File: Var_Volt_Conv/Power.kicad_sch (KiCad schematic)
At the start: 64 parts

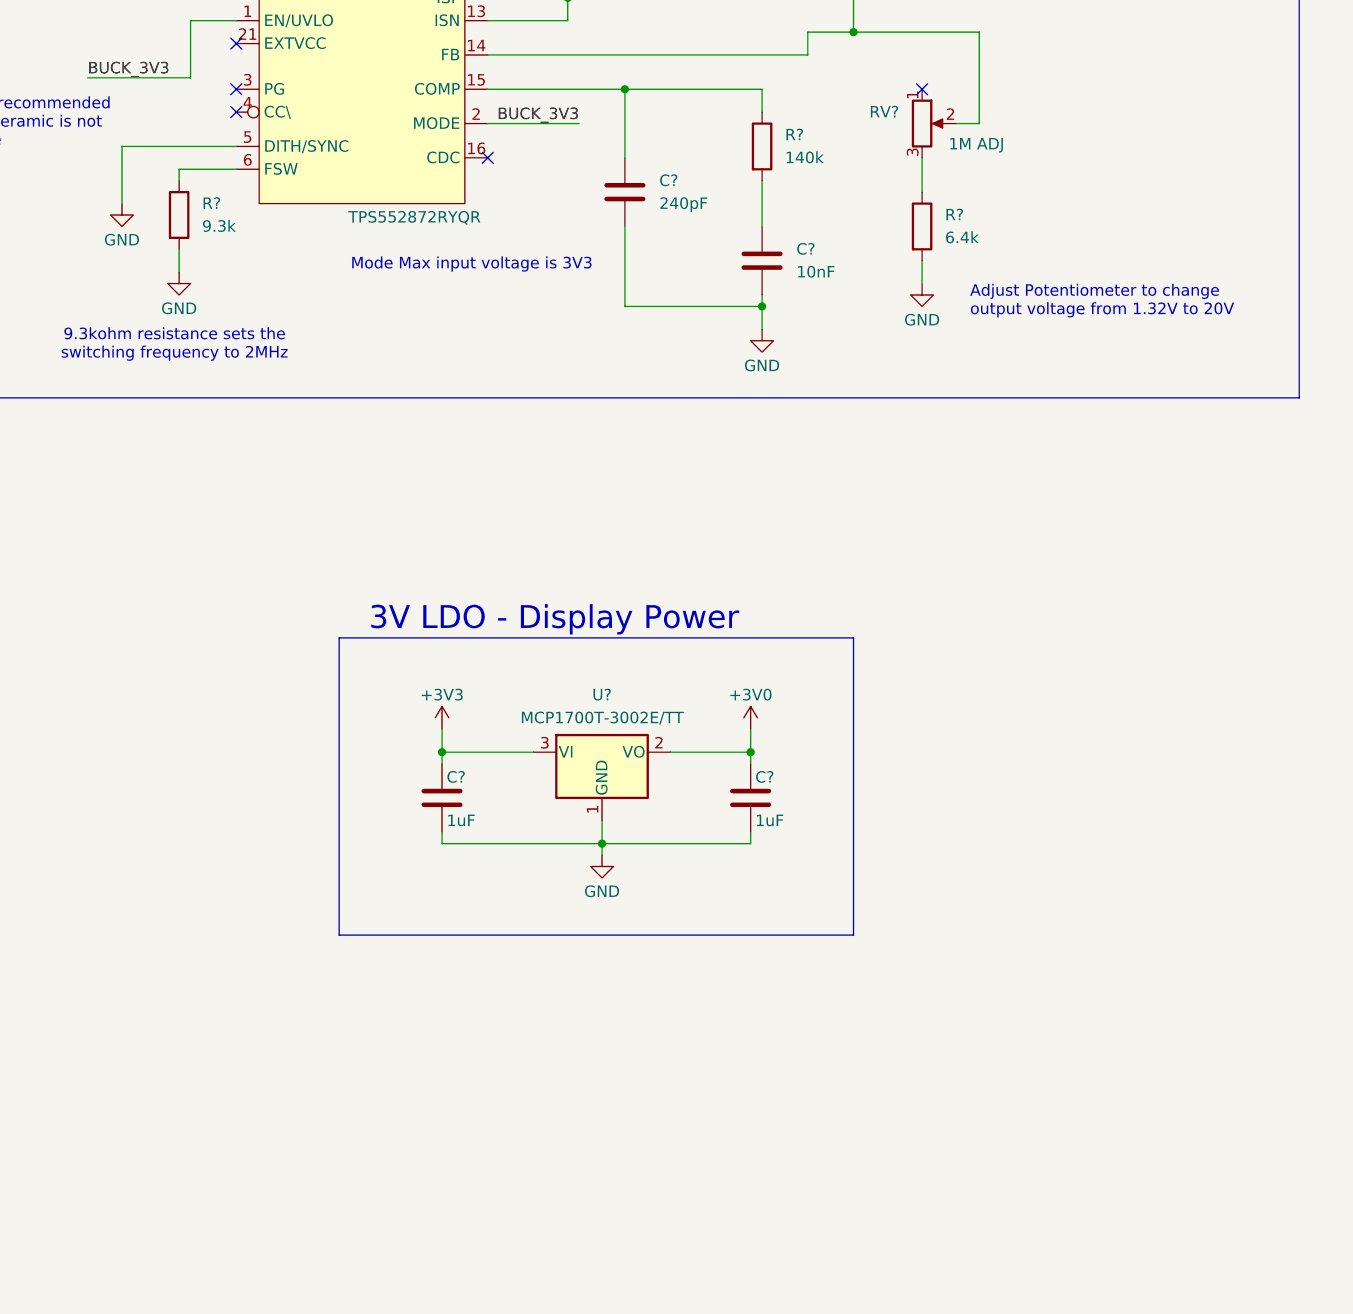
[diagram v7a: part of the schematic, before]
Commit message: Added microcontroller notes, and power indicator LED
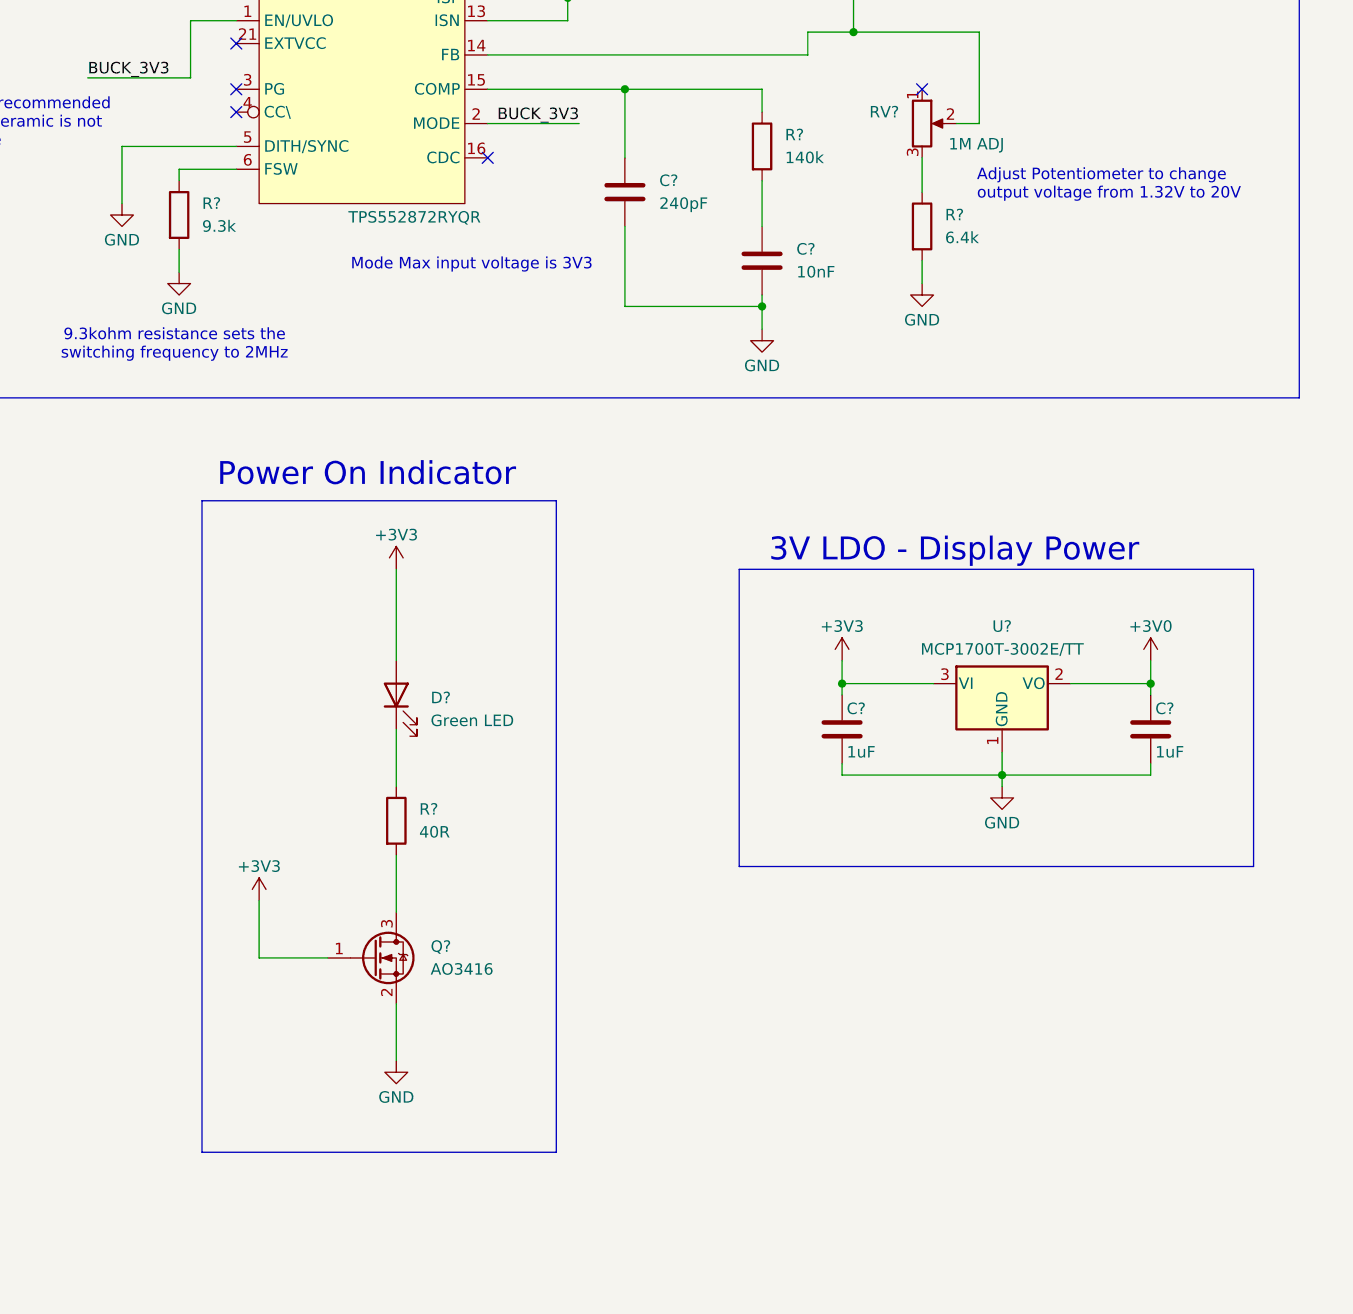
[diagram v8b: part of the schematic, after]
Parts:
- added D?: Green LED, LED_SMD:LED_0603_1608Metric, symbol Device:LED
- added Q?: AO3416, Package_TO_SOT_SMD:SOT-23, symbol Transistor_FET:AO3400A
- added R?: 40R, symbol Device:R
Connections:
- net +3V3: now also D?.2 (A), Q?.1 (G)
- net GND: now also Q?.2 (S)
- new net: D?.1 (K), R?.1
- new net: Q?.3 (D), R?.2
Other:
- note added: "Power On Indicator"
- moved on the sheet: C?, U?
